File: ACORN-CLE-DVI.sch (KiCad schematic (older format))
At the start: 2 parts, among them J1 HDMI_A, U1 PI3HDX511D

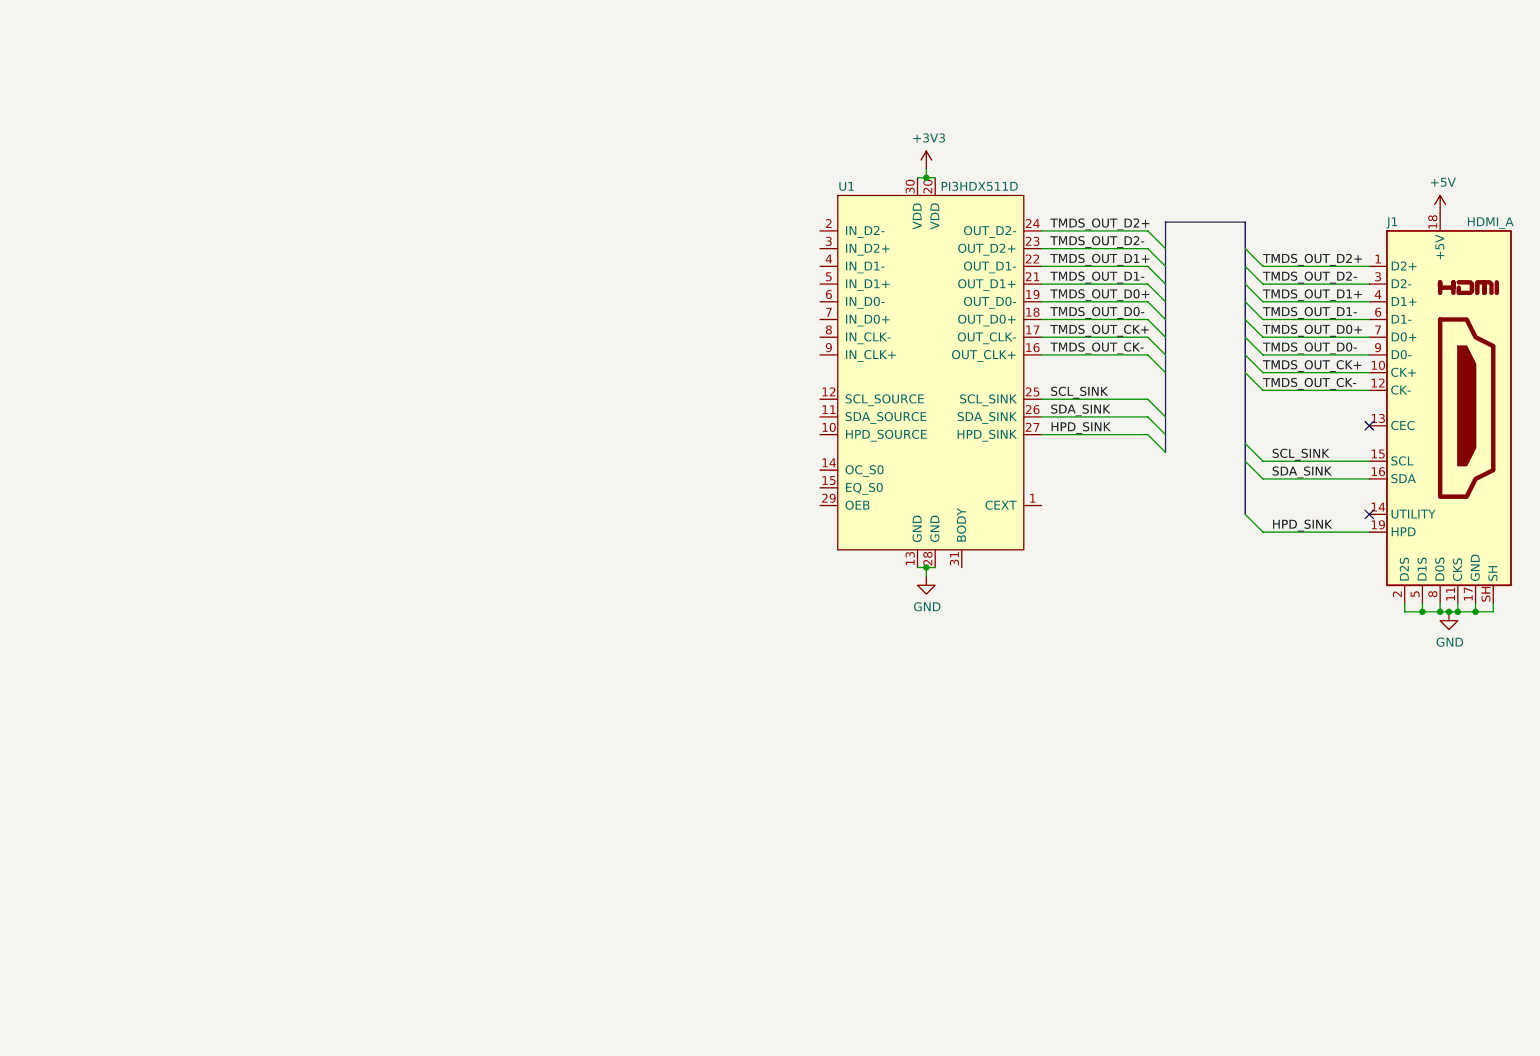
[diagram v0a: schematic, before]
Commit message: schematic done, most of board routing
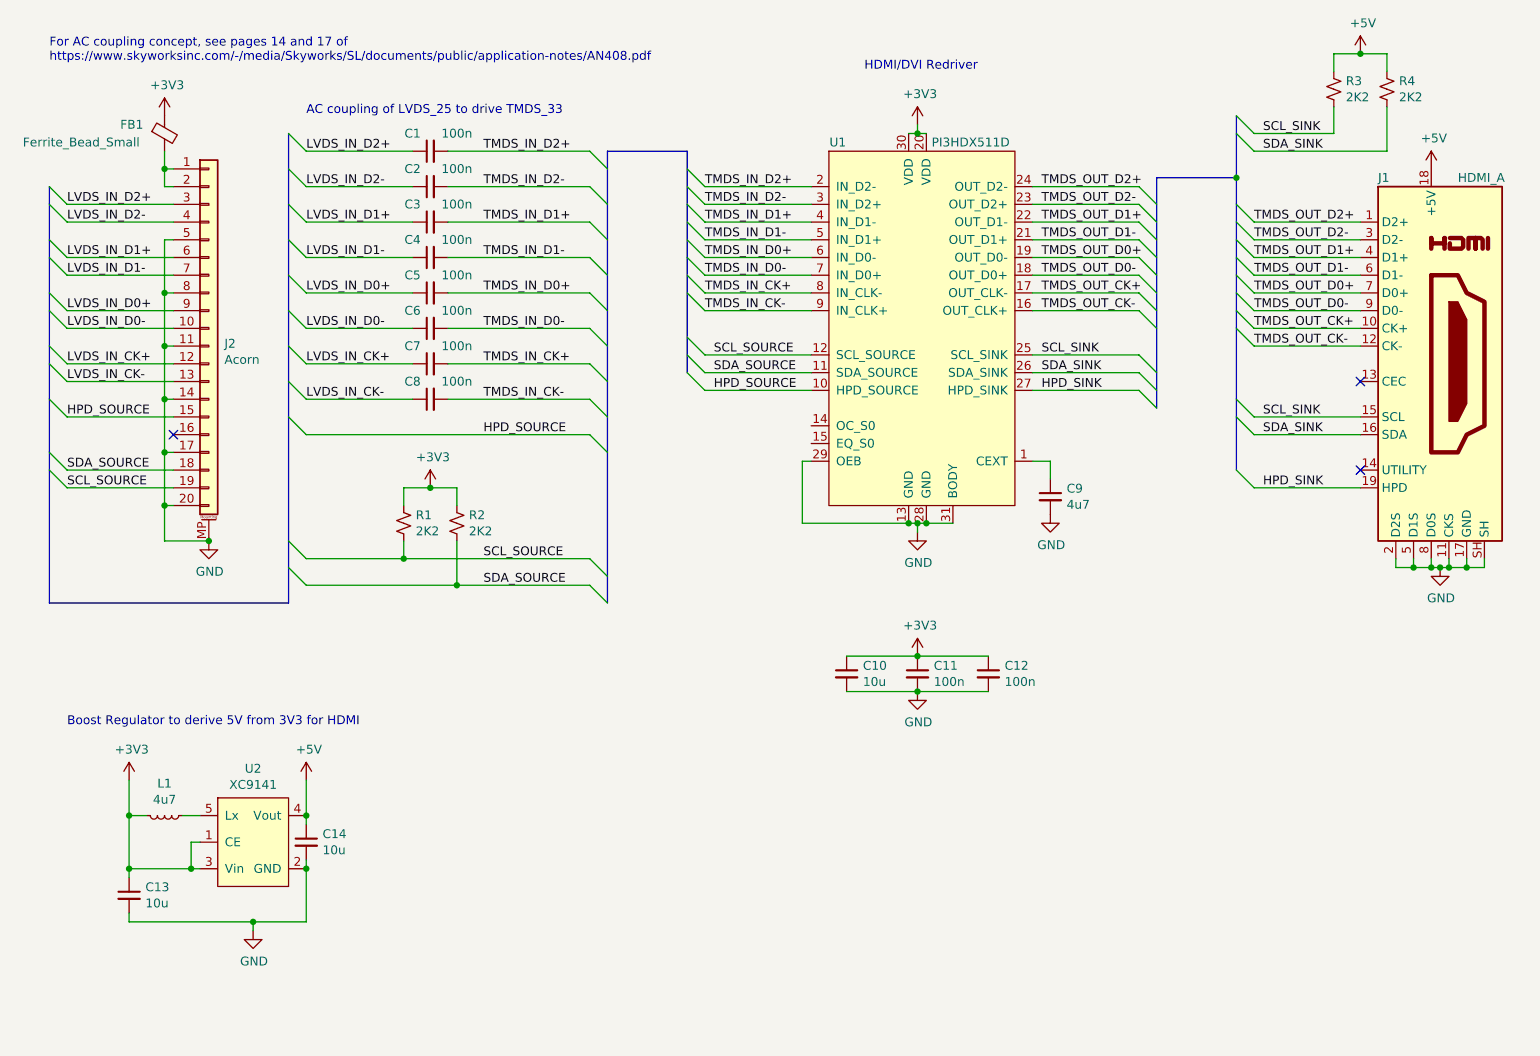
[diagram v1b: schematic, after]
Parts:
- added C1, C11, C12, C2, C3, C4, C5, C6, C7, C8: 100n, Capacitor_SMD:C_0402_1005Metric, symbol Device:C_Small
- added C10, C13, C14: 10u, Capacitor_SMD:C_0402_1005Metric, symbol Device:C_Small
- added C9: 4u7, Capacitor_SMD:C_0402_1005Metric, symbol Device:C_Small
- added FB1: Ferrite_Bead_Small, Inductor_SMD:L_0603_1608Metric, symbol Device:Ferrite_Bead_Small
- added J2: Acorn, ACORN-CLE-HDMI:Hirose_DF52-20S-0.8H_1x20-1MP_P0.80mm_Horizontal, symbol Connector_Generic_MountingPin:Conn_01x20_MountingPin
- added L1: 4u7, Inductor_SMD:L_1008_2520Metric, symbol Device:L_Small
- added R1, R2, R3, R4: 2K2, Resistor_SMD:R_0402_1005Metric, symbol Device:R_Small_US
- added U2: XC9141, Package_TO_SOT_SMD:SOT-23-5, symbol Parts:XC9141
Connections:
- net +3V3: now also C10.1, C11.1, C12.1, C13.1, FB1.1, L1.2, R1.1, R2.1, U2.1 (CE), U2.3 (Vin)
- net +5V: now also C14.1, R3.1, R4.1, U2.4 (Vout)
- net GND: now also U1.29 (OEB), U1.31 (BODY), C10.2, C11.2, C12.2, C13.2, C14.2, C9.2, J2.11 (Pin_11), J2.14 (Pin_14), J2.17 (Pin_17), J2.20 (Pin_20), J2.5 (Pin_5), J2.8 (Pin_8), J2.MP (MountPin), U2.2 (GND)
- net SCL_SINK: now also R3.2
- net SDA_SINK: now also R4.2
- net at U1.1 (CEXT): now also C9.1
- net HPD_SOURCE: now reaches U1.10 (HPD_SOURCE)
- net HPD_SOURCE: now also J2.15 (Pin_15)
- net SDA_SOURCE: now reaches U1.11 (SDA_SOURCE)
- net SDA_SOURCE: now also J2.18 (Pin_18), R2.2
- net SCL_SOURCE: now reaches U1.12 (SCL_SOURCE)
- net SCL_SOURCE: now also J2.19 (Pin_19), R1.2
- net TMDS_IN_D2+: now reaches U1.2 (IN_D2-)
- net TMDS_IN_D2+: now also C1.2
- net TMDS_IN_D2-: now reaches U1.3 (IN_D2+)
- net TMDS_IN_D2-: now also C2.2
- net TMDS_IN_D1+: now reaches U1.4 (IN_D1-)
- net TMDS_IN_D1+: now also C3.2
- net TMDS_IN_D1-: now reaches U1.5 (IN_D1+)
- net TMDS_IN_D1-: now also C4.2
- net TMDS_IN_D0+: now reaches U1.6 (IN_D0-)
- net TMDS_IN_D0+: now also C5.2
- net TMDS_IN_D0-: now reaches U1.7 (IN_D0+)
- net TMDS_IN_D0-: now also C6.2
- net TMDS_IN_CK+: now reaches U1.8 (IN_CLK-)
- net TMDS_IN_CK+: now also C7.2
- net TMDS_IN_CK-: now reaches U1.9 (IN_CLK+)
- net TMDS_IN_CK-: now also C8.2
- new net: FB1.2, J2.1 (Pin_1), J2.2 (Pin_2)
- new net: L1.1, U2.5 (Lx)
- new net LVDS_IN_CK+: C7.1, J2.12 (Pin_12)
- new net LVDS_IN_CK-: C8.1, J2.13 (Pin_13)
- new net LVDS_IN_D0+: C5.1, J2.9 (Pin_9)
- new net LVDS_IN_D0-: C6.1, J2.10 (Pin_10)
- new net LVDS_IN_D1+: C3.1, J2.6 (Pin_6)
- new net LVDS_IN_D1-: C4.1, J2.7 (Pin_7)
- new net LVDS_IN_D2+: C1.1, J2.3 (Pin_3)
- new net LVDS_IN_D2-: C2.1, J2.4 (Pin_4)
- no-connect marks 2 -> 3
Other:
- note added: "AC coupling of LVDS_25 to drive TMDS_33"
- note added: "Boost Regulator to derive 5V from 3V3 for HDMI"
- note added: "For AC coupling concept, see pages 14 and 17 of\nhttps://www.skyworksinc.com/-/media/Skyworks/SL/documents/public/application-notes/AN408.pdf"
- note added: "HDMI/DVI Redriver"
- moved on the sheet: J1, U1

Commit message: functionally complete, need to verify before buying
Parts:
- added JP1: Equalization, Jumper:SolderJumper-3_P1.3mm_Open_RoundedPad1.0x1.5mm_NumberLabels, symbol Jumper:SolderJumper_3_Open
- added JP2: Pre-emphasis, Jumper:SolderJumper-3_P1.3mm_Open_RoundedPad1.0x1.5mm_NumberLabels, symbol Jumper:SolderJumper_3_Open
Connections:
- net +3V3: now also JP1.1 (A), JP2.3 (B)
- net GND: now also JP1.3 (B), JP2.1 (A)
- net OC: now reaches U1.14 (OC_S0)
- net OC: now also JP2.2 (C)
- net EQ: now reaches U1.15 (EQ_S0)
- net EQ: now also JP1.2 (C)
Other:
- moved on the sheet: C1, C10, C11, C12, C13, C14, C2, C3, C4, C5, C6, C7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

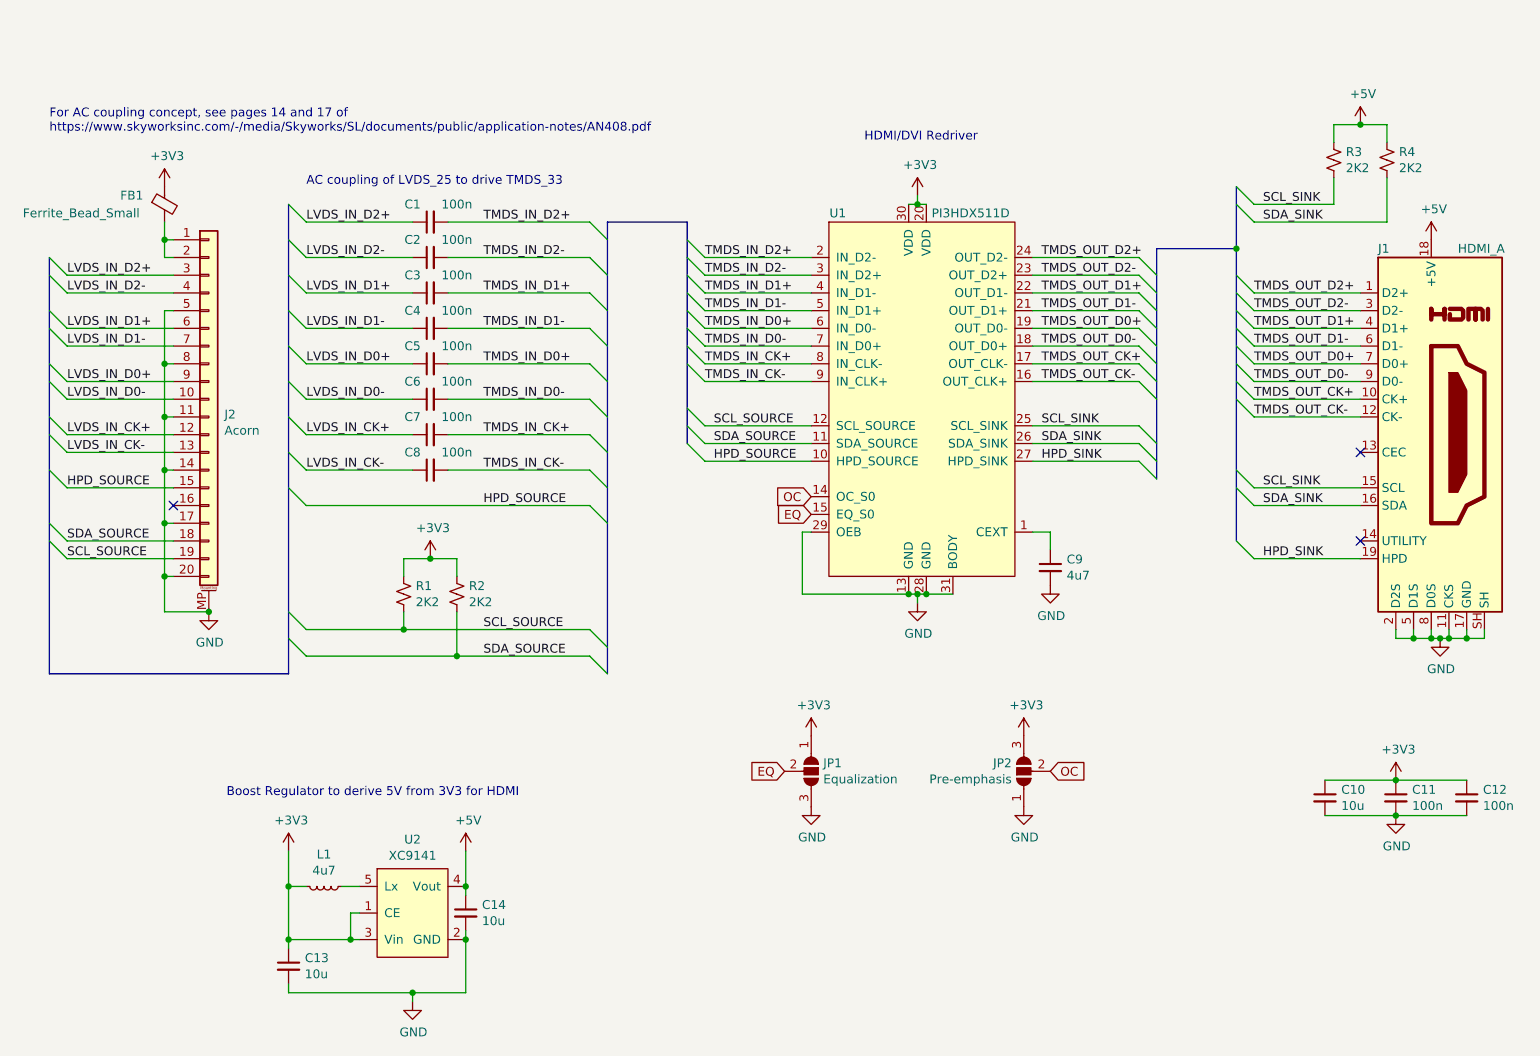
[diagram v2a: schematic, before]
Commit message: add datasheets and digikey part numbers
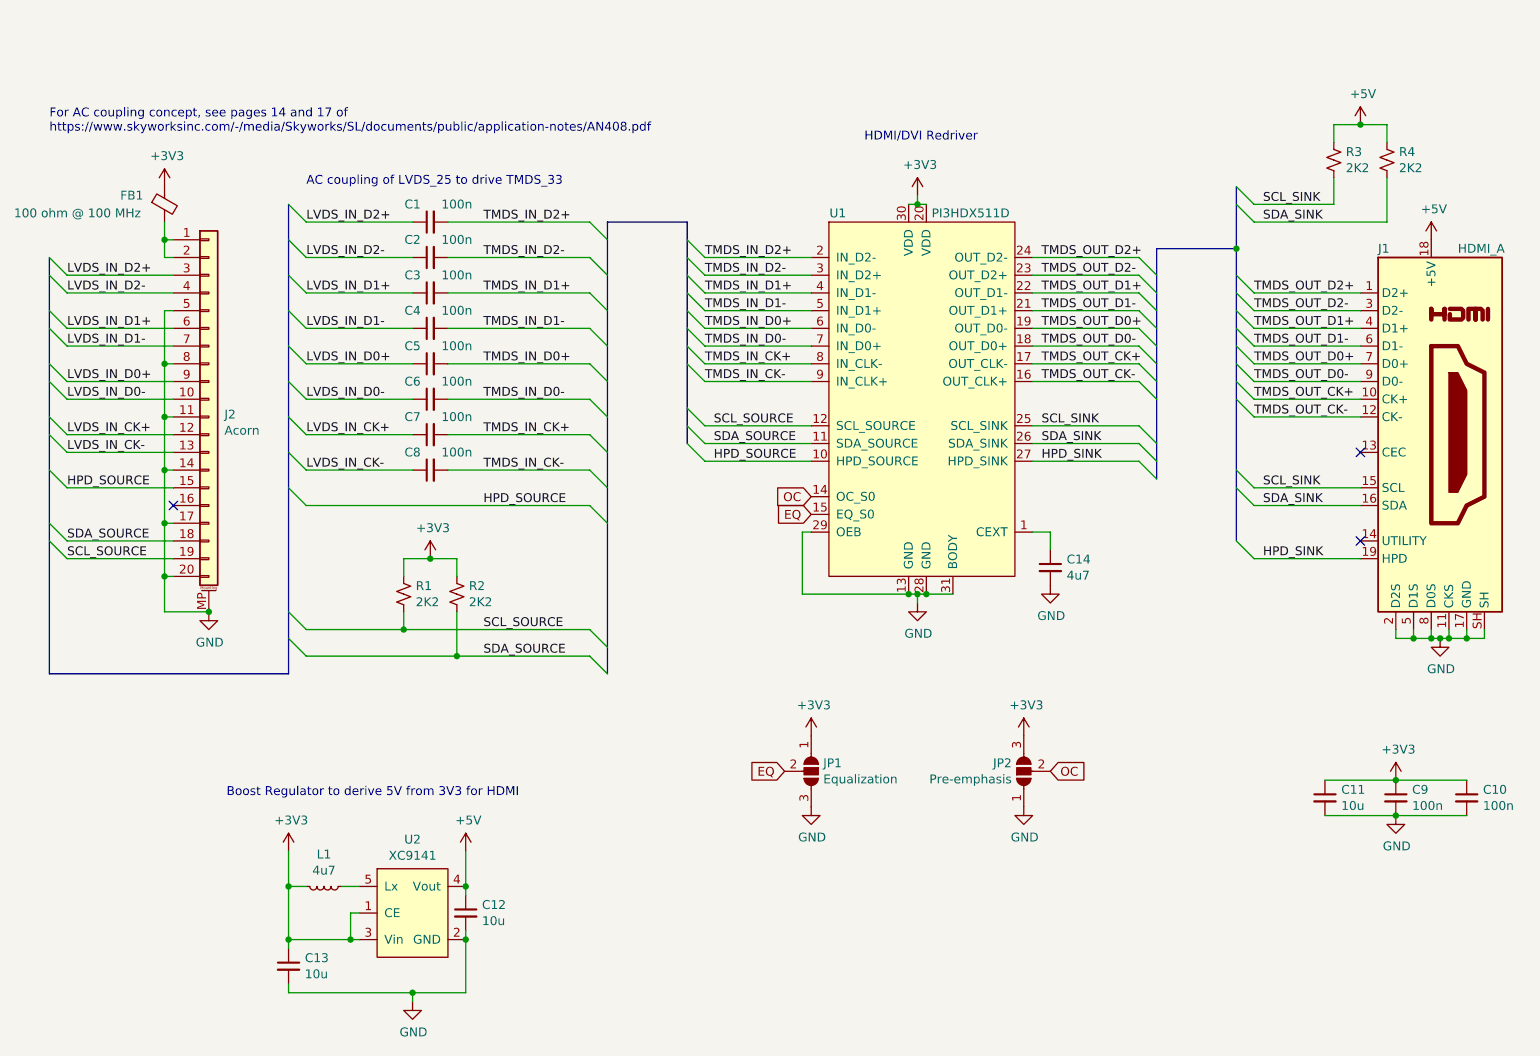
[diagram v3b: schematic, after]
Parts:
- C1, C2, C3, C4, C5, C6, C7, C8: Digikey_Link (none) -> https://www.digikey.com/en/products/detail/samsung-electro-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; Digikey_PN (none) -> 1276-1043-2-ND
- C10: renamed from C12; Digikey_Link (none) -> https://www.digikey.com/en/products/detail/samsung-electro-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; Digikey_PN (none) -> 1276-1043-2-ND
- C11: renamed from C10; Digikey_Link (none) -> https://www.digikey.com/en/products/detail/murata-electroni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; Digikey_PN (none) -> 490-GRM155R61A106ME11DTR-ND
- C12: renamed from C14; Digikey_Link (none) -> https://www.digikey.com/en/products/detail/murata-electroni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; Digikey_PN (none) -> 490-GRM155R61A106ME11DTR-ND
- C13: Digikey_Link (none) -> https://www.digikey.com/en/products/detail/murata-electroni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; Digikey_PN (none) -> 490-GRM155R61A106ME11DTR-ND
- C14: renamed from C9; Digikey_Link (none) -> https://www.digikey.com/en/products/detail/samsung-electro-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; Digikey_PN (none) -> 1276-1482-2-ND
- C9: renamed from C11; Digikey_Link (none) -> https://www.digikey.com/en/products/detail/samsung-electro-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; Digikey_PN (none) -> 1276-1043-2-ND
- FB1: value Ferrite_Bead_Small -> 100 ohm @ 100 MHz; Digikey_Link (none) -> https://www.digikey.com/en/products/detail/murata-electroni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; Digikey_PN (none) -> 490-5448-2-ND
- J1: Digikey_Link (none) -> https://www.digikey.com/en/products/detail/cnc-tech/2000-1-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; Digikey_PN (none) -> 1175-1703-ND
- J2: Digikey_Link (none) -> https://www.digikey.com/en/products/detail/hirose-electric-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; Digikey_PN (none) -> H125108TR-ND
- L1: Digikey_Link (none) -> https://www.digikey.com/en/products/detail/abracon-llc/AIML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; Digikey_PN (none) -> 535-12797-2-ND
- R1, R2, R3, R4: Digikey_Link (none) -> https://www.digikey.com/en/products/detail/yageo/RC0402JR-0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; Digikey_PN (none) -> 311-2.2KJRTR-ND
- U1: Digikey_Link (none) -> https://www.digikey.com/en/products/detail/diodes-incorpora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; Digikey_PN (none) -> PI3HDX511DZLEXDITR-ND
- U2: Digikey_Link (none) -> https://www.digikey.com/en/products/detail/torex-semiconduc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; Digikey_PN (none) -> 893-1369-2-ND
